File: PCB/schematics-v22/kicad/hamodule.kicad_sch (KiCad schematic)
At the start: 85 parts, among them J1 GND|5V, J10 Conn_01x02_Male, J11 USB_C_Receptacle_USB2.0, J12 2604-1104, J13 EspSense, J2 2604-1102, J3 Conn_01x02_Male, J4 USB | PS, J5 Conn_01x02_Male, J6 GND|3.3V, J7 Current Jumper, J8 EspRelays, J9 2604-1104, K1 AQG12205, K2 AQG12205, K3 AQG12205, K4 AQG12205, SW1 Switch, SW2 Switch, U1 LD1117AV33, U2 ESP32-S3-WROOM-2, U3 ULN2003A, U4 USBLC6-2SC6, U5 LDA210-PDIP, U6 LDA210-PDIP, U7 SHT4x

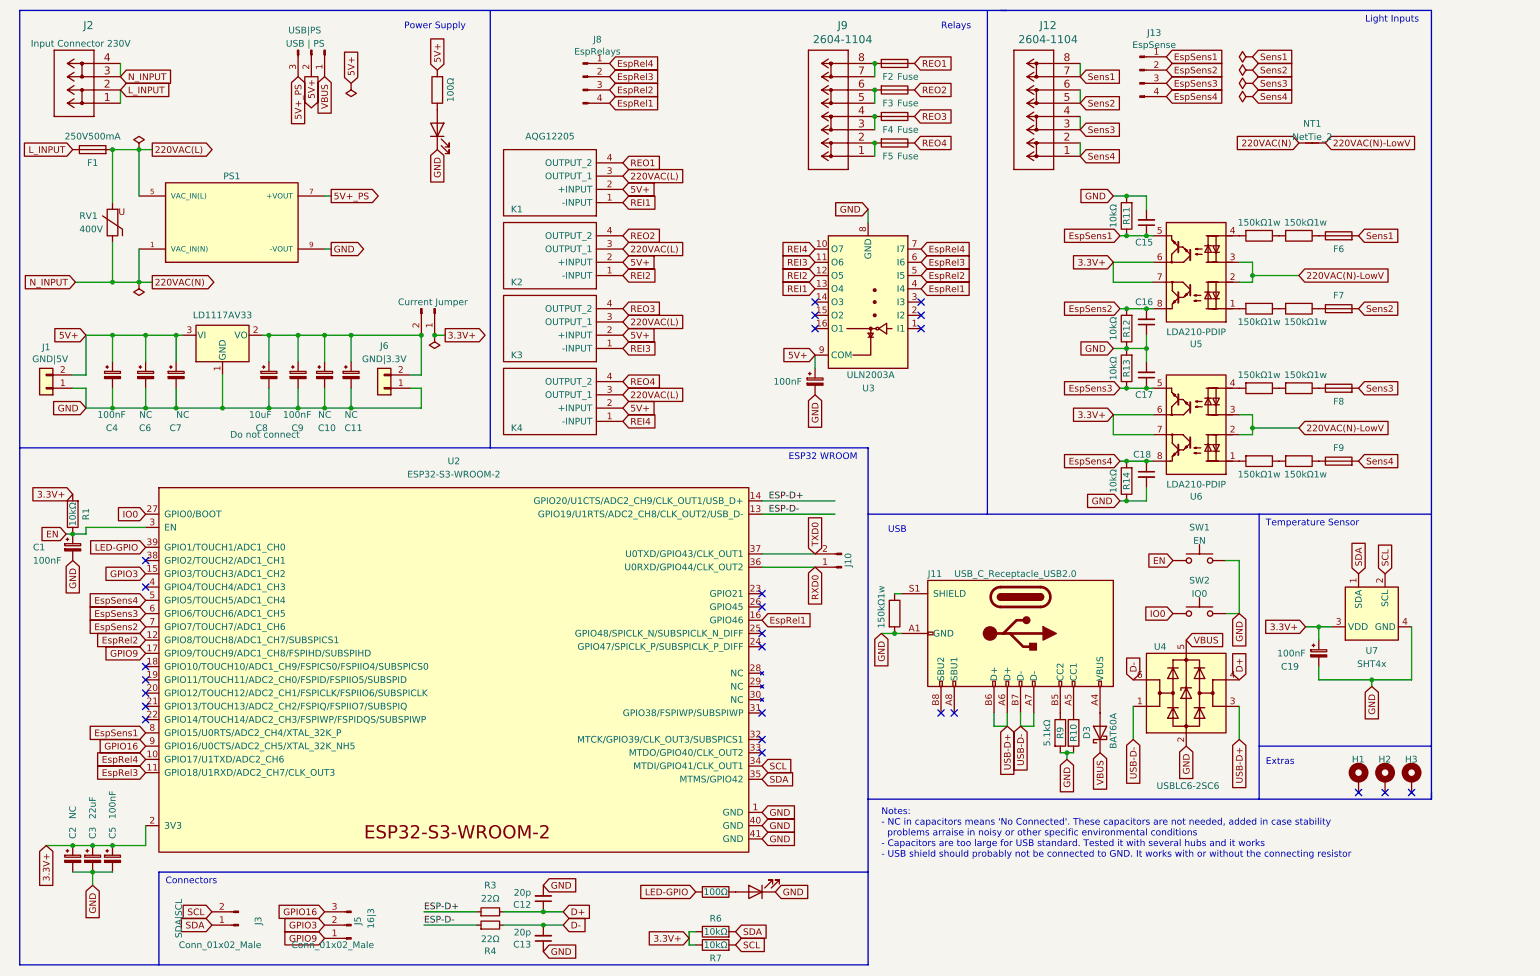
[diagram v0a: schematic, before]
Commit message: improving schematics, removing global variables and use wires instead to make it clear how the circuit is working; trying to move inputs to the left, output to the right
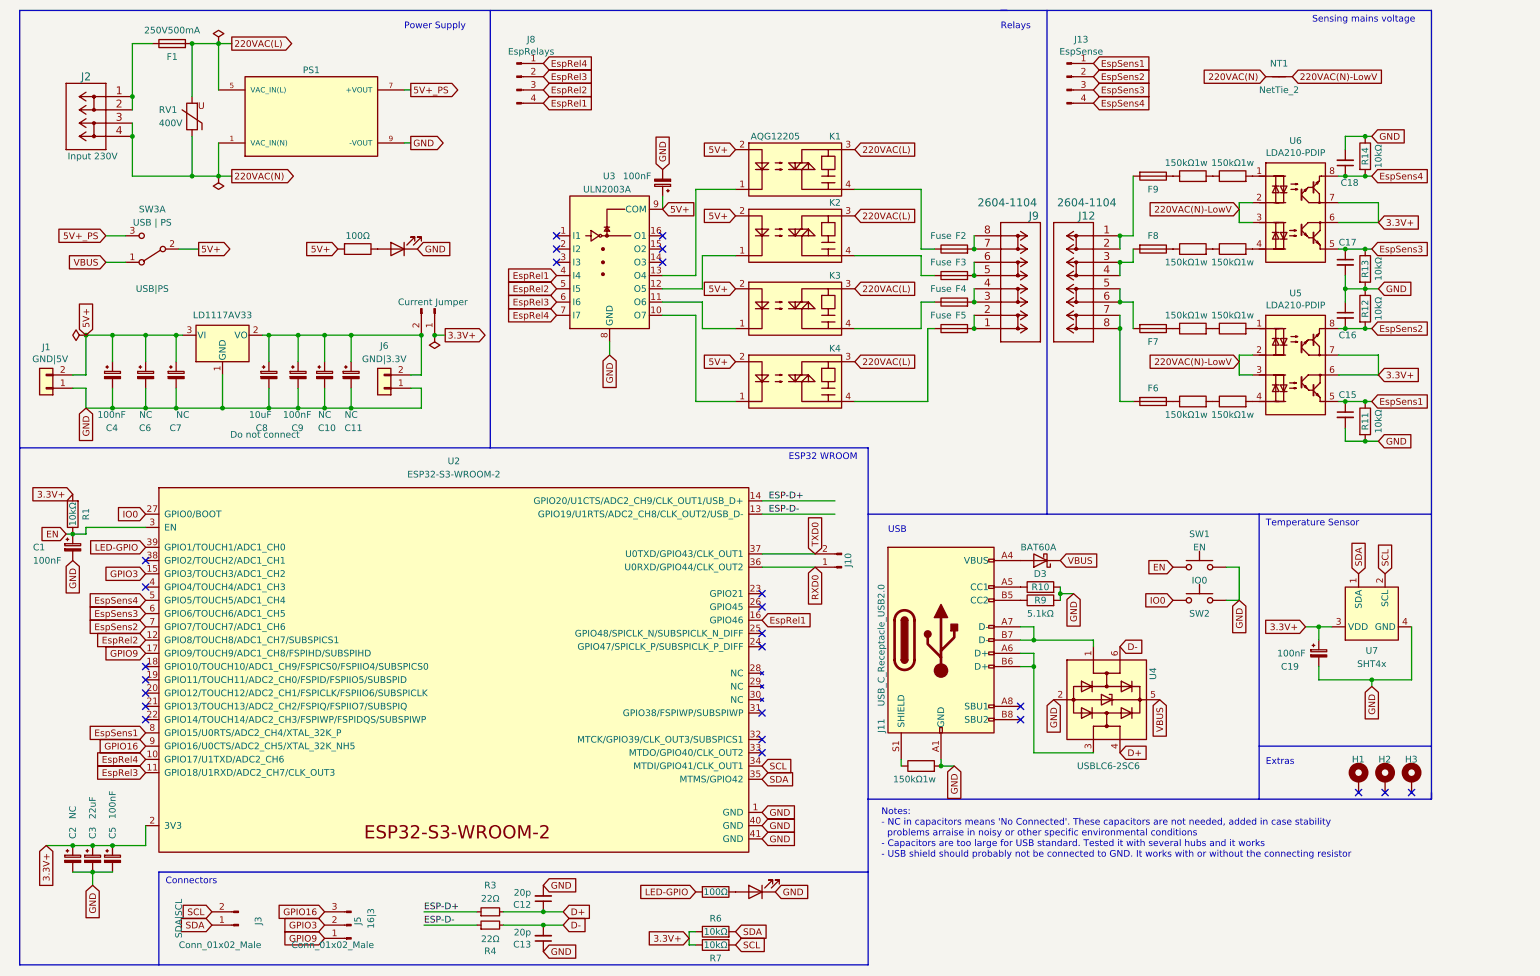
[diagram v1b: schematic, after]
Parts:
- removed J4: USB | PS, Connector_PinHeader_2.54mm:PinHeader_1x03_P2.54mm_Vertical, symbol Connector:Conn_01x03_Male
- added SW3: USB | PS, Connector_PinHeader_2.54mm:PinHeader_1x03_P2.54mm_Vertical, symbol Switch:SW_DPDT_x2
- J2: Text Input Connector 230V -> Input 230V
- K1: footprint AQG12205:AQG12205 -> AQG12205
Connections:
- net 5V+: now also SW3.2 (B)
- net 5V+_PS: now also SW3.3 (C)
- net VBUS: now also SW3.1 (A)
- net L_INPUT: no longer names the net of F1.1, J2.1, J2.2
- net REI1: no longer names the net of K1.1, U3.13 (O4)
- net REI2: no longer names the net of K2.1, U3.12 (O5)
- net REI3: no longer names the net of K3.1, U3.11 (O6)
- net REI4: no longer names the net of K4.1, U3.10 (O7)
- net REO1: no longer names the net of F2.1, K1.4
- net REO2: no longer names the net of F3.1, K2.4
- net REO3: no longer names the net of F4.1, K3.4
- net REO4: no longer names the net of F5.1, K4.4
- net Sens1: no longer names the net of F6.2, J12.7, J12.8
- net Sens2: no longer names the net of F7.2, J12.5, J12.6
- net Sens3: no longer names the net of F8.2, J12.3, J12.4
- net Sens4: no longer names the net of F9.2, J12.1, J12.2
- net USB-D+: no longer names the net of J11.A6 (D+), J11.B6 (D+), U4.3 (I/O2)
- net USB-D-: no longer names the net of J11.A7 (D-), J11.B7 (D-), U4.1 (I/O1)
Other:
- note added: "Sensing mains voltage"
- note removed: "Light Inputs"
- moved on the sheet: C15, C16, C17, C18, D3, F1, F2, F3, F4, F6, F7, F8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

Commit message: [V22] Making schematics cleaner + Production files
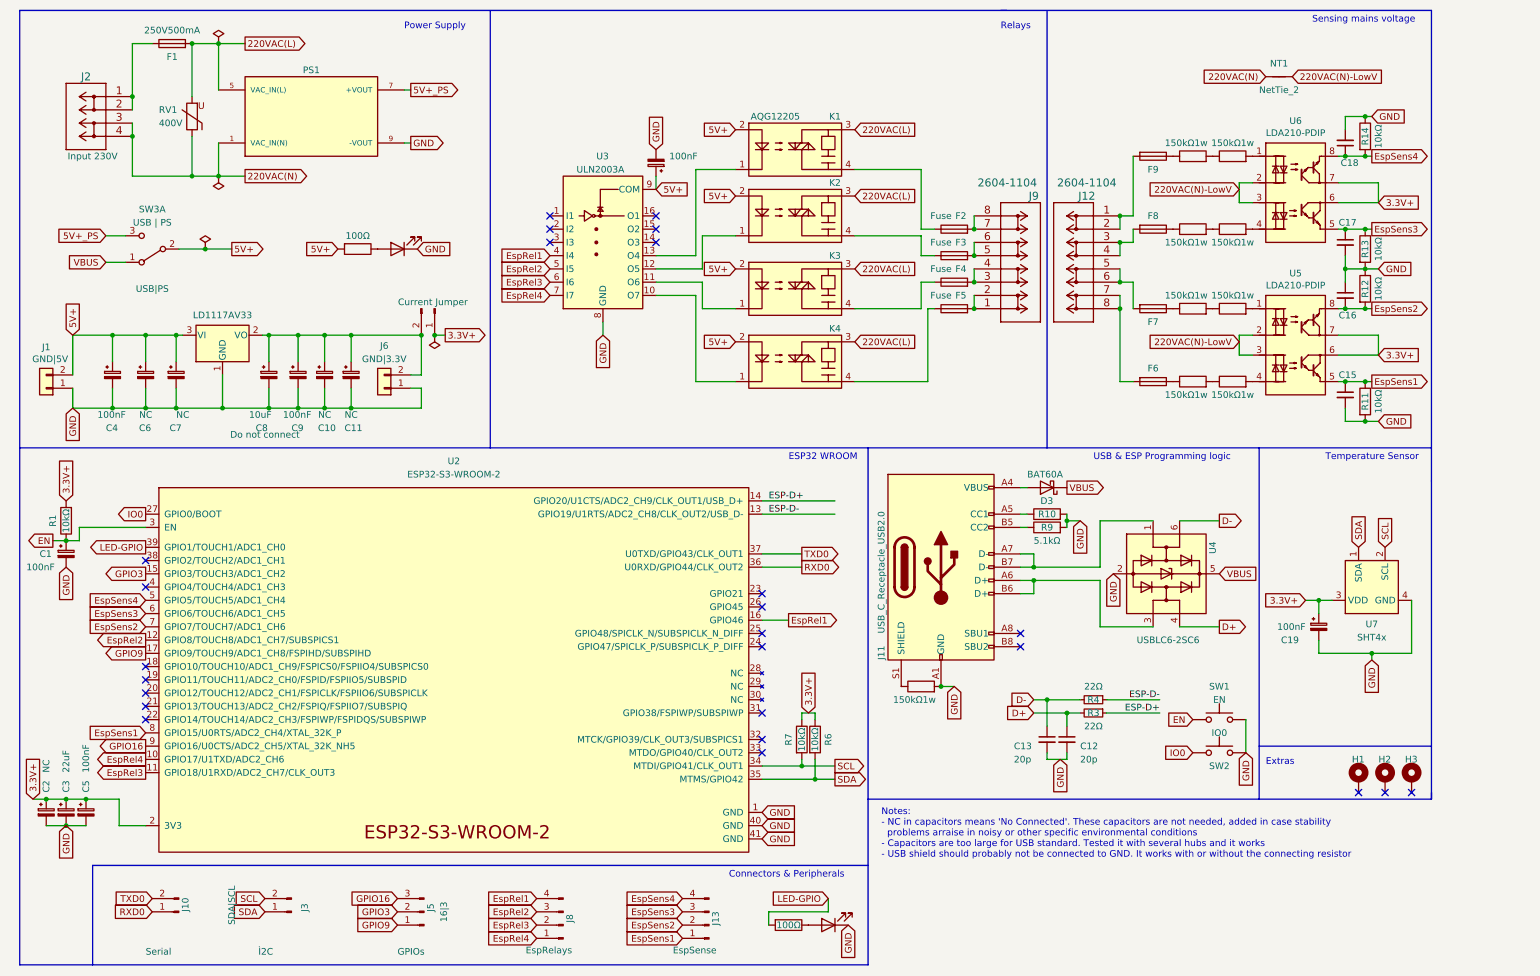
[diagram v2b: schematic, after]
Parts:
- C1, C14, C19, C4, C5, C9: LCSC (none) -> C14663
- C12, C13: JLCPCB (none) -> C1648
- C15, C16, C17, C18, C3: LCSC (none) -> C59461
- D1, D2: LCSC (none) -> C2297
- D3: JLCPCB (none) -> C124187; LCSC (none) -> C124187
- J10: value Conn_01x02_Male -> Serial
- J11: LCSC (none) -> C167321
- J3: value Conn_01x02_Male -> Ì2C
- J5: value Conn_01x02_Male -> GPIOs
- K1: footprint AQG12205 -> AQG12205:AQG12205
- R1, R11, R12, R13, R14, R6, R7: LCSC (none) -> C25804
- R10, R9: LCSC (none) -> C23186
- R15, R16, R17, R18, R19, R20, R21, R22, R8: LCSC (none) -> C25719
- R2, R5: LCSC (none) -> C17408
- R3, R4: JLCPCB (none) -> C23345
- SW1, SW2: LCSC (none) -> C318884
- U3: LCSC (none) -> C7512
- U4: JLCPCB (none) -> C2827654; LCSC (none) -> C2827654
- U7: LCSC (none) -> C2909890
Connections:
- net D-: now also C13.1; no longer C13.2
- net GND: now also C13.2; no longer C13.1
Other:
- note added: "Connectors & Peripherals"
- note added: "USB & ESP Programming logic"
- note removed: "Connectors"
- note removed: "USB"
- moved on the sheet: C1, C12, C13, C15, C16, C17, C18, C19, C2, C3, C5, D3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

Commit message: adding leds to indicate relays operation
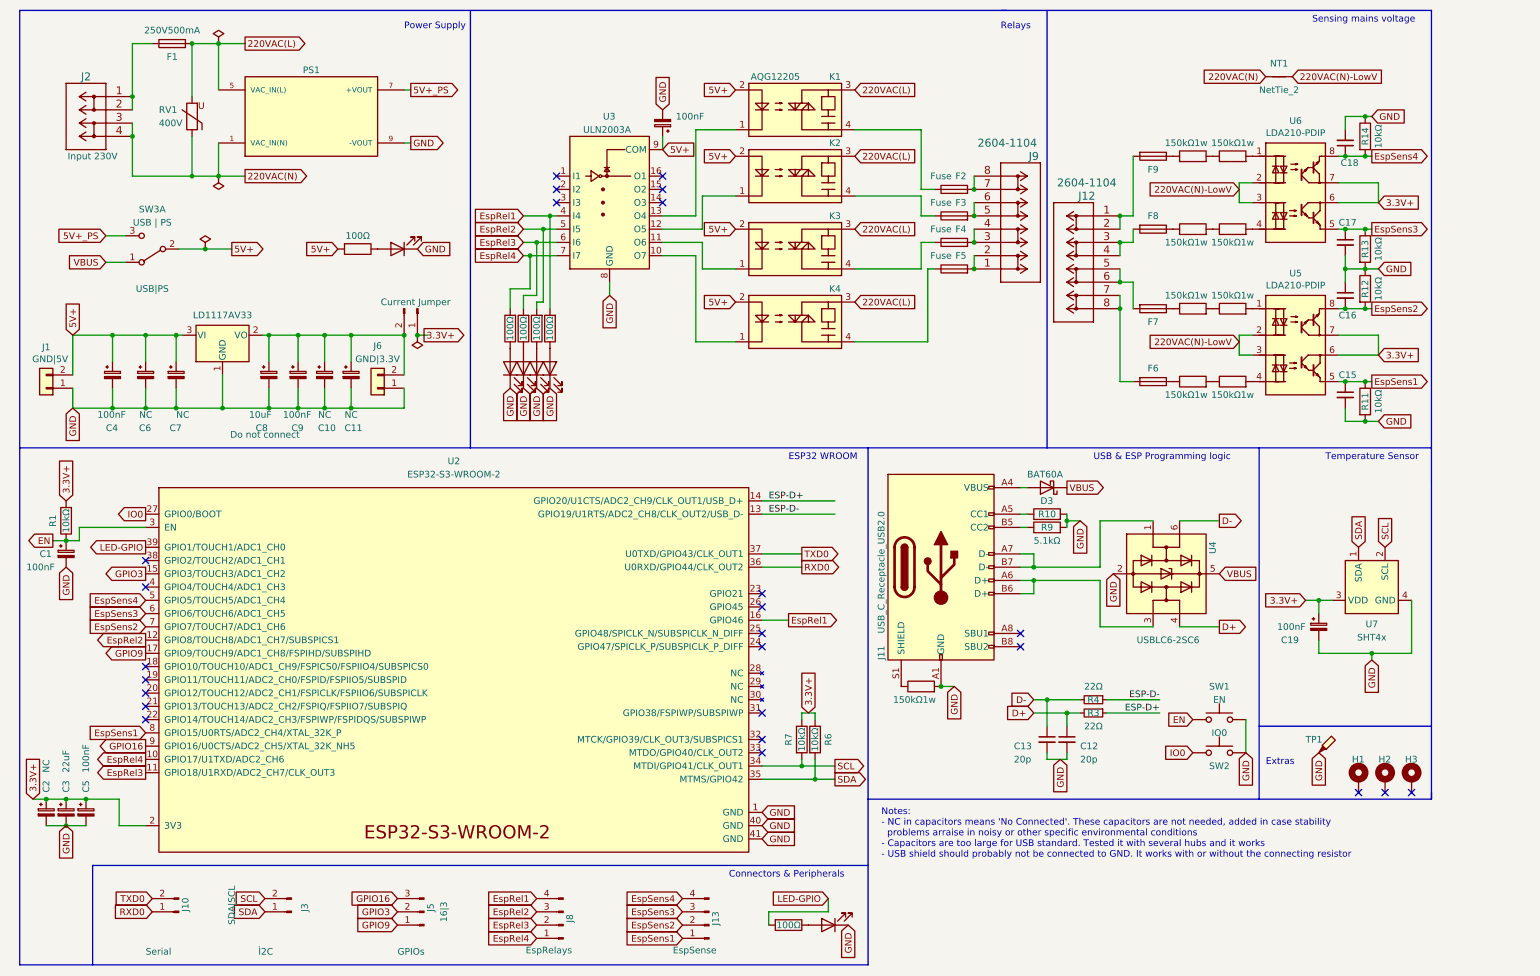
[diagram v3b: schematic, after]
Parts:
- added D4, D5, D6, D7: LED, LED_SMD:LED_0603_1608Metric, symbol Device:LED
- added R23, R24, R25, R26: 100Ω, Resistor_SMD:R_0603_1608Metric_Pad0.98x0.95mm_HandSolder, symbol Device:R
- added TP1: TestPoint_Probe, TestPoint:TestPoint_THTPad_1.0x1.0mm_Drill0.5mm, symbol Connector:TestPoint_Probe
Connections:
- net EspRel1: now also R23.2
- net EspRel2: now also R24.2
- net EspRel3: now also R25.2
- net EspRel4: now also R26.2
- net GND: now also D4.1 (K), D5.1 (K), D6.1 (K), D7.1 (K), TP1.1
- new net: D5.2 (A), R24.1
- new net: D4.2 (A), R23.1
- new net: D7.2 (A), R26.1
- new net: D6.2 (A), R25.1
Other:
- moved on the sheet: F2, F3, F4, F5, J6, J9, K1, K2, K3, K4, U3

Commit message: Use VBus for ESD before BAT diode; Adding 2 more GPIO; Adding more caps
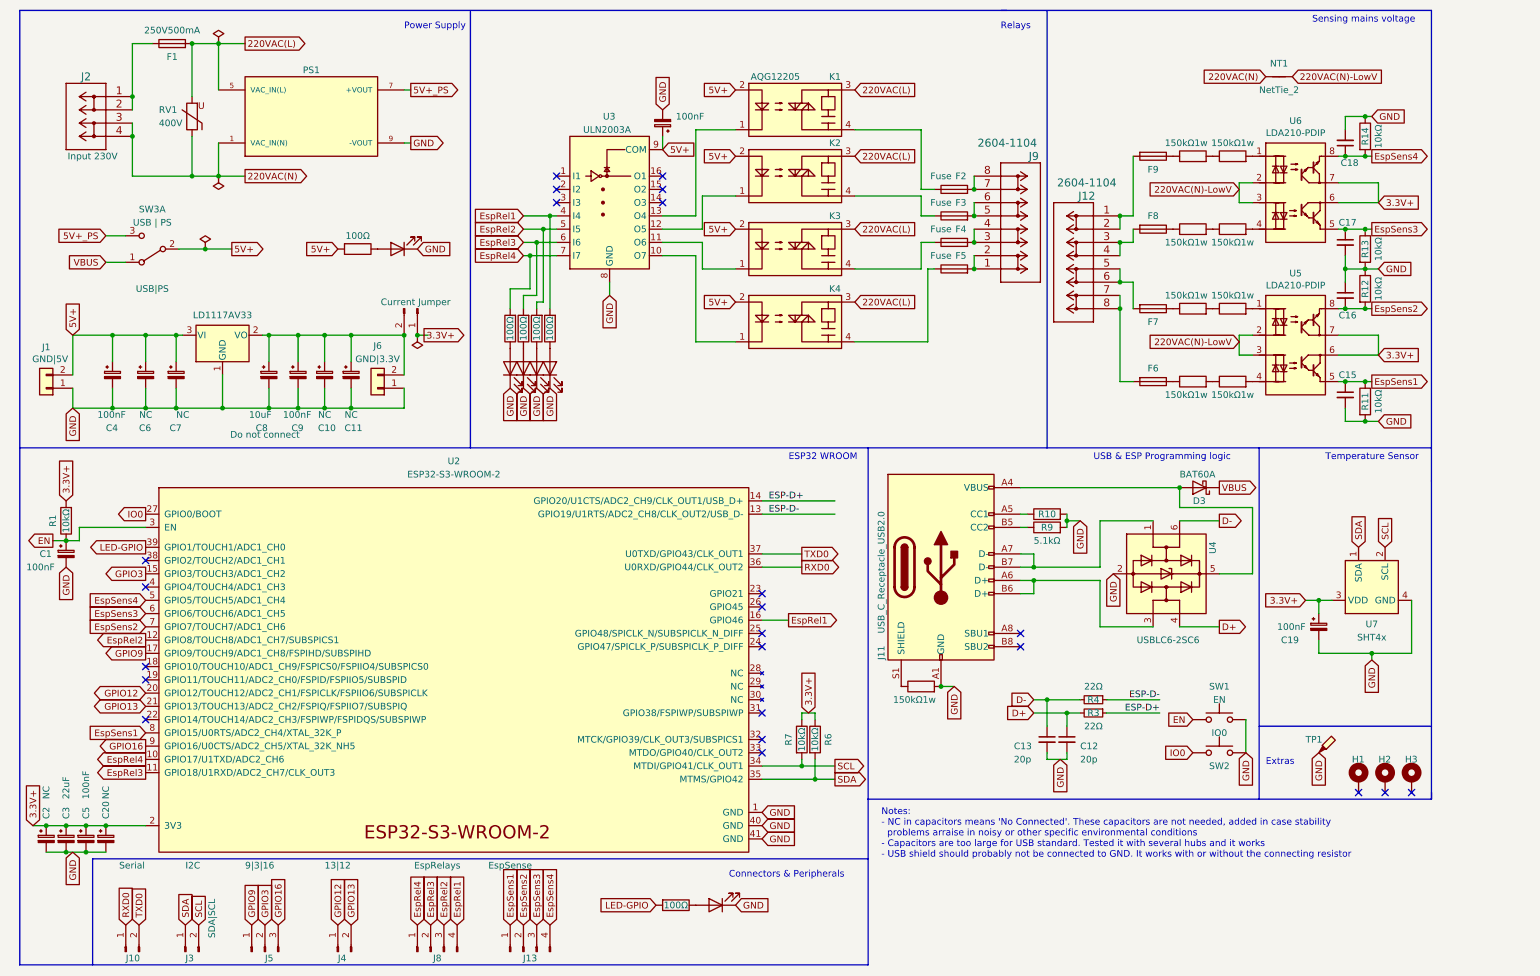
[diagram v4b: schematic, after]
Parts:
- added C20: NC, Capacitor_SMD:C_0805_2012Metric_Pad1.18x1.45mm_HandSolder, symbol Device:C_Polarized_Small
- added J4: 13|12, Connector_PinHeader_2.54mm:PinHeader_1x02_P2.54mm_Vertical, symbol Connector:Conn_01x02_Male
- C2: footprint Capacitor_SMD:C_0603_1608Metric_Pad1.08x0.95mm_HandSolder -> Capacitor_SMD:C_1206_3216Metric_Pad1.33x1.80mm_HandSolder
- J3: value Ì2C -> I2C
- J5: value GPIOs -> 9|3|16; PcbText 16|3 -> 9|16|3
- TP1: value TestPoint_Probe -> GND
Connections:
- net 3.3V+: now also C20.1
- net GND: now also C20.2
- net VBUS: no longer U4.5 (VBUS)
- net at D3.2 (A), J11.A4 (VBUS), J11.A9 (VBUS)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: now also U4.5 (VBUS)
- net GPIO12: now reaches U2.20 (GPIO12/TOUCH12/ADC2_CH1/FSPICLK/FSPIIO6/SUBSPICLK)
- net GPIO12: now also J4.1 (Pin_1)
- net GPIO13: now reaches U2.21 (GPIO13/TOUCH13/ADC2_CH2/FSPIQ/FSPIIO7/SUBSPIQ)
- net GPIO13: now also J4.2 (Pin_2)
- no-connect marks 25 -> 23
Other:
- moved on the sheet: C2, C3, C5, D3, J10, J13, J3, J5, J8
